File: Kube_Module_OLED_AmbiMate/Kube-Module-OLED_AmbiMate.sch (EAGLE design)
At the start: 9 parts

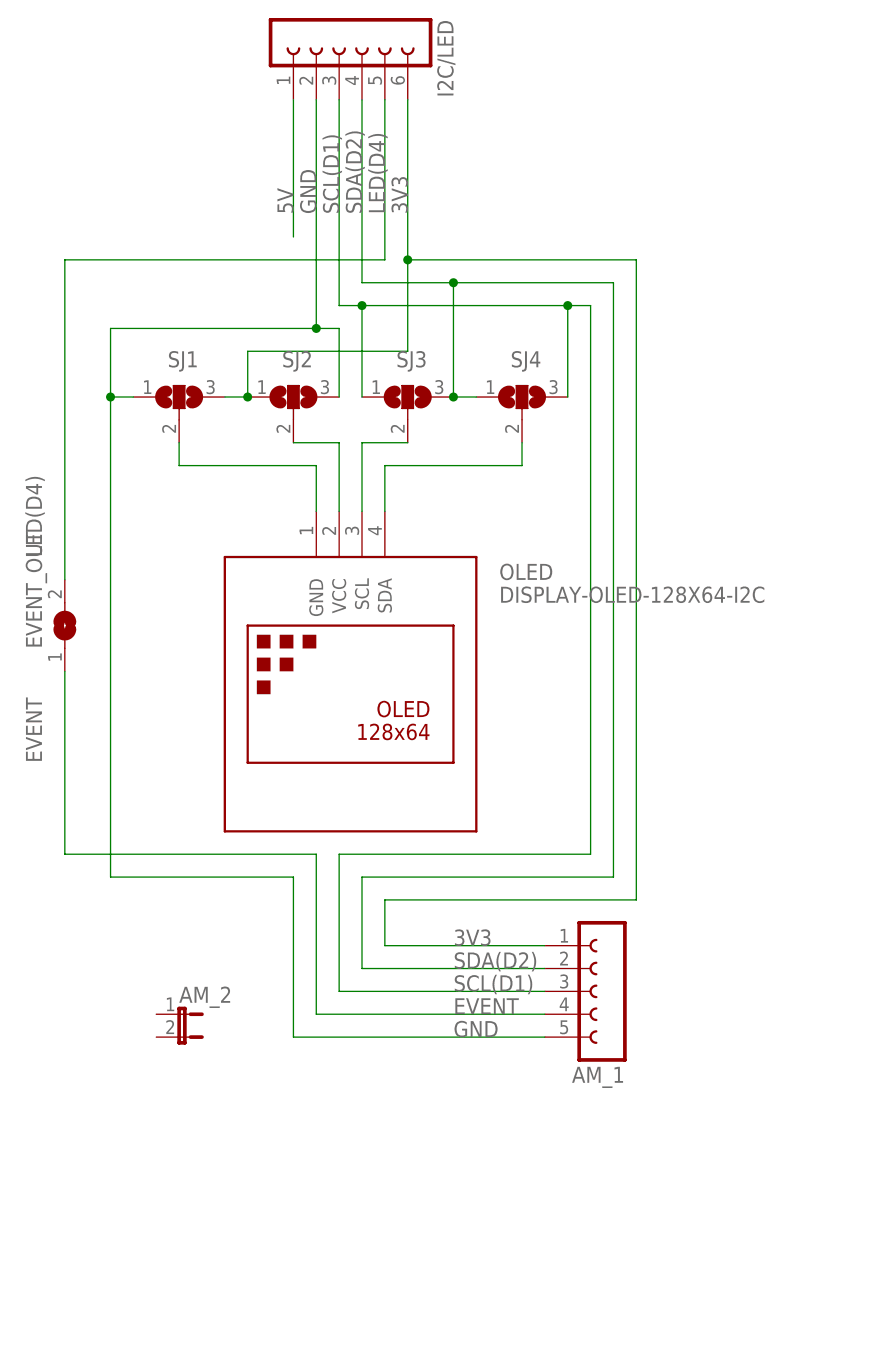
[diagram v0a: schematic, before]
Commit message: Mods to OLED board to get rid of EVENT_OUT (causes boot issues since D4 needs to be held HI)
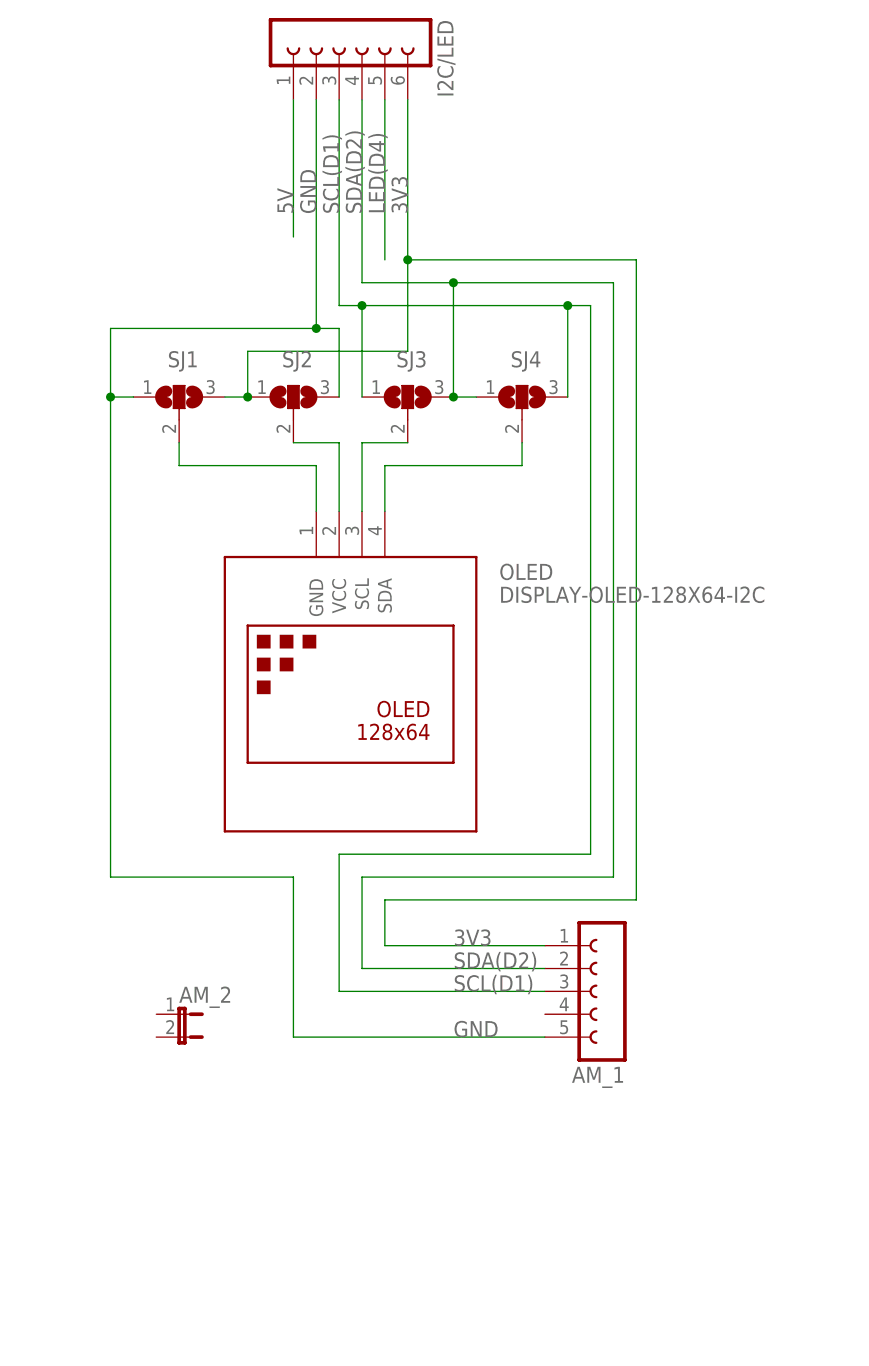
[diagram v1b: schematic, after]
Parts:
- removed EVENT_OUT: (no value), jumper:SJ
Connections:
- removed net EVENT: AM_1.4, EVENT_OUT.1
- net LED(D4): no longer EVENT_OUT.2
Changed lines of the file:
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@@
 <?xml version="1.0" encoding="utf-8"?>
 <!DOCTYPE eagle SYSTEM "eagle.dtd">
-<eagle version="9.3.0">
+<eagle version="9.4.2">
 <drawing>
 <settings>
@@
 <part name="AM_1" library="con-lsta" library_urn="urn:adsk.eagle:library:161" deviceset="FE05-1" device="" package3d_urn="urn:adsk.eagle:package:8190/1"/>
 <part name="AM_2" library="jumper" library_urn="urn:adsk.eagle:library:252" deviceset="JP1E" device="" package3d_urn="urn:adsk.eagle:package:15455/1"/>
-<part name="EVENT_OUT" library="jumper" library_urn="urn:adsk.eagle:library:252" deviceset="SJ" device="" package3d_urn="urn:adsk.eagle:package:15471/1"/>
 </parts>
 <sheets>
@@
 <attribute name="NAME" x="58.42" y="-16.51" size="1.778" layer="95"/>
 <attribute name="VALUE" x="58.42" y="-23.495" size="1.778" layer="96"/>
-</instance>
-<instance part="EVENT_OUT" gate="1" x="45.72" y="25.4" smashed="yes" rot="R90">
-<attribute name="NAME" x="43.18" y="22.86" size="1.778" layer="95" rot="R90"/>
-<attribute name="VALUE" x="49.53" y="22.86" size="1.778" layer="96" rot="R90"/>
 </instance>
 </instances>
@@
 </segment>
 </net>
-<net name="EVENT" class="0">
-<segment>
-<pinref part="AM_1" gate="G$1" pin="4"/>
-<label x="88.9" y="-17.78" size="1.778" layer="95"/>
-<wire x1="99.06" y1="-17.78" x2="73.66" y2="-17.78" width="0.1524" layer="91"/>
-<wire x1="73.66" y1="-17.78" x2="73.66" y2="0" width="0.1524" layer="91"/>
-<wire x1="73.66" y1="0" x2="45.72" y2="0" width="0.1524" layer="91"/>
-<wire x1="45.72" y1="0" x2="45.72" y2="20.32" width="0.1524" layer="91"/>
-<pinref part="EVENT_OUT" gate="1" pin="1"/>
-<label x="43.18" y="10.16" size="1.778" layer="95" rot="R90"/>
-</segment>
-</net>
 <net name="5V" class="0">
 <segment>
@@
 <pinref part="I2C/LED" gate="G$1" pin="5"/>
 <wire x1="81.28" y1="66.04" x2="81.28" y2="83.82" width="0.1524" layer="91"/>
-<wire x1="45.72" y1="66.04" x2="81.28" y2="66.04" width="0.1524" layer="91"/>
-<wire x1="45.72" y1="30.48" x2="45.72" y2="66.04" width="0.1524" layer="91"/>
 <label x="81.28" y="71.12" size="1.778" layer="95" rot="R90"/>
-<pinref part="EVENT_OUT" gate="1" pin="2"/>
-<label x="43.18" y="33.02" size="1.778" layer="95" rot="R90"/>
-</segment>
-</net>
+</segment>
+</net>

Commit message: Added BMx280 sensor to OLED Board
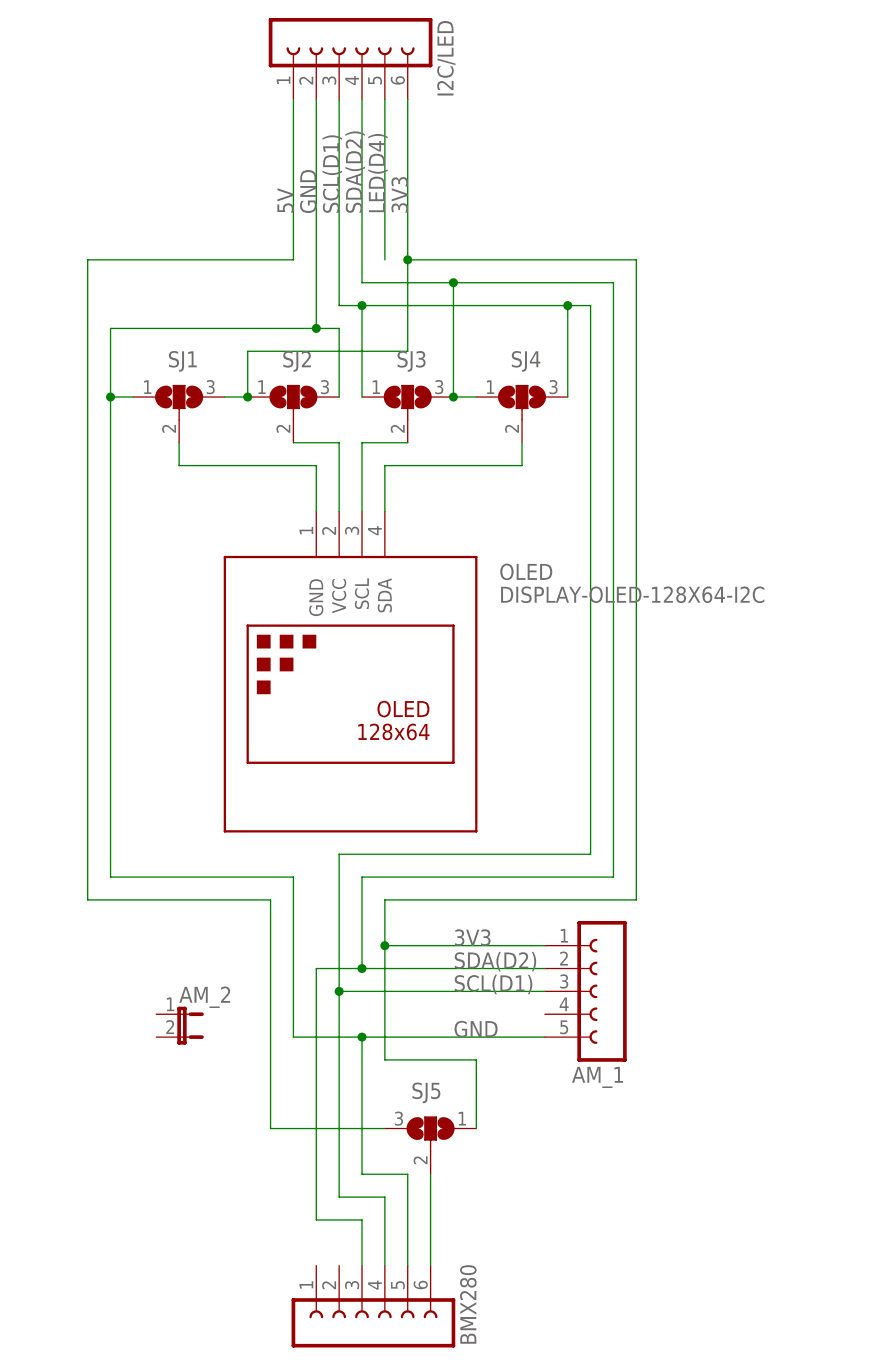
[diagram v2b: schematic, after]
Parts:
- added BMX280: (no value), con-lsta:FE06-1
- added SJ5: (no value), jumper:SJ2W
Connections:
- new net BMX_VCC: BMX280.6, SJ5.2
- net 3V3: now also SJ5.1
- net 5V: now also SJ5.3
- net GND: now also BMX280.5
- net SCL(D1): now also BMX280.4
- net SDA(D2): now also BMX280.3
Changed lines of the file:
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@@
 <?xml version="1.0" encoding="utf-8"?>
 <!DOCTYPE eagle SYSTEM "eagle.dtd">
-<eagle version="9.4.2">
+<eagle version="9.5.2">
 <drawing>
 <settings>
@@
 <part name="AM_1" library="con-lsta" library_urn="urn:adsk.eagle:library:161" deviceset="FE05-1" device="" package3d_urn="urn:adsk.eagle:package:8190/1"/>
 <part name="AM_2" library="jumper" library_urn="urn:adsk.eagle:library:252" deviceset="JP1E" device="" package3d_urn="urn:adsk.eagle:package:15455/1"/>
+<part name="BMX280" library="con-lsta" library_urn="urn:adsk.eagle:library:161" deviceset="FE06-1" device="" package3d_urn="urn:adsk.eagle:package:8191/1"/>
+<part name="SJ5" library="jumper" library_urn="urn:adsk.eagle:library:252" deviceset="SJ2W" device="" package3d_urn="urn:adsk.eagle:package:15474/1"/>
 </parts>
 <sheets>
@@
 <attribute name="NAME" x="58.42" y="-16.51" size="1.778" layer="95"/>
 <attribute name="VALUE" x="58.42" y="-23.495" size="1.778" layer="96"/>
+</instance>
+<instance part="BMX280" gate="G$1" x="78.74" y="-53.34" smashed="yes" rot="MR90">
+<attribute name="VALUE" x="68.58" y="-54.61" size="1.778" layer="96" rot="MR90"/>
+<attribute name="NAME" x="89.662" y="-54.61" size="1.778" layer="95" rot="MR90"/>
+</instance>
+<instance part="SJ5" gate="G$1" x="86.36" y="-30.48" smashed="yes" rot="MR90">
+<attribute name="NAME" x="84.201" y="-25.4" size="1.778" layer="95" rot="MR180"/>
+<attribute name="VALUE" x="84.455" y="-27.94" size="1.778" layer="96" rot="MR90"/>
 </instance>
 </instances>
@@
 <pinref part="AM_1" gate="G$1" pin="5"/>
 <label x="88.9" y="-20.32" size="1.778" layer="95"/>
-<wire x1="99.06" y1="-20.32" x2="71.12" y2="-20.32" width="0.1524" layer="91"/>
+<wire x1="99.06" y1="-20.32" x2="78.74" y2="-20.32" width="0.1524" layer="91"/>
+<wire x1="78.74" y1="-20.32" x2="71.12" y2="-20.32" width="0.1524" layer="91"/>
 <wire x1="71.12" y1="-20.32" x2="71.12" y2="-2.54" width="0.1524" layer="91"/>
 <wire x1="71.12" y1="-2.54" x2="50.8" y2="-2.54" width="0.1524" layer="91"/>
+<wire x1="78.74" y1="-20.32" x2="78.74" y2="-35.56" width="0.1524" layer="91"/>
+<wire x1="78.74" y1="-35.56" x2="83.82" y2="-35.56" width="0.1524" layer="91"/>
+<junction x="78.74" y="-20.32"/>
+<pinref part="BMX280" gate="G$1" pin="5"/>
+<wire x1="83.82" y1="-35.56" x2="83.82" y2="-45.72" width="0.1524" layer="91"/>
 </segment>
 </net>
@@
 <wire x1="99.06" y1="-15.24" x2="76.2" y2="-15.24" width="0.1524" layer="91"/>
 <label x="88.9" y="-15.24" size="1.778" layer="95"/>
+<pinref part="BMX280" gate="G$1" pin="4"/>
+<wire x1="81.28" y1="-45.72" x2="81.28" y2="-38.1" width="0.1524" layer="91"/>
+<wire x1="81.28" y1="-38.1" x2="76.2" y2="-38.1" width="0.1524" layer="91"/>
+<wire x1="76.2" y1="-38.1" x2="76.2" y2="-15.24" width="0.1524" layer="91"/>
+<junction x="76.2" y="-15.24"/>
 </segment>
 </net>
@@
 <label x="88.9" y="-12.7" size="1.778" layer="95"/>
 <wire x1="78.74" y1="-12.7" x2="99.06" y2="-12.7" width="0.1524" layer="91"/>
+<wire x1="78.74" y1="-12.7" x2="73.66" y2="-12.7" width="0.1524" layer="91"/>
+<junction x="78.74" y="-12.7"/>
+<wire x1="73.66" y1="-12.7" x2="73.66" y2="-40.64" width="0.1524" layer="91"/>
+<wire x1="73.66" y1="-40.64" x2="78.74" y2="-40.64" width="0.1524" layer="91"/>
+<pinref part="BMX280" gate="G$1" pin="3"/>
+<wire x1="78.74" y1="-40.64" x2="78.74" y2="-45.72" width="0.1524" layer="91"/>
 </segment>
 </net>
@@
 <wire x1="99.06" y1="-10.16" x2="81.28" y2="-10.16" width="0.1524" layer="91"/>
 <label x="88.9" y="-10.16" size="1.778" layer="95"/>
+<wire x1="81.28" y1="-10.16" x2="81.28" y2="-22.86" width="0.1524" layer="91"/>
+<junction x="81.28" y="-10.16"/>
+<wire x1="81.28" y1="-22.86" x2="91.44" y2="-22.86" width="0.1524" layer="91"/>
+<pinref part="SJ5" gate="G$1" pin="1"/>
+<wire x1="91.44" y1="-22.86" x2="91.44" y2="-30.48" width="0.1524" layer="91"/>
 </segment>
 </net>
@@
 <segment>
 <pinref part="I2C/LED" gate="G$1" pin="1"/>
-<wire x1="71.12" y1="83.82" x2="71.12" y2="68.58" width="0.1524" layer="91"/>
+<wire x1="71.12" y1="83.82" x2="71.12" y2="66.04" width="0.1524" layer="91"/>
 <label x="71.12" y="71.12" size="1.778" layer="95" rot="R90"/>
+<wire x1="71.12" y1="66.04" x2="48.26" y2="66.04" width="0.1524" layer="91"/>
+<wire x1="48.26" y1="66.04" x2="48.26" y2="-5.08" width="0.1524" layer="91"/>
+<wire x1="48.26" y1="-5.08" x2="68.58" y2="-5.08" width="0.1524" layer="91"/>
+<wire x1="68.58" y1="-5.08" x2="68.58" y2="-30.48" width="0.1524" layer="91"/>
+<pinref part="SJ5" gate="G$1" pin="3"/>
+<wire x1="68.58" y1="-30.48" x2="81.28" y2="-30.48" width="0.1524" layer="91"/>
 </segment>
 </net>
@@
 </segment>
 </net>
+<net name="BMX_VCC" class="0">
+<segment>
+<pinref part="BMX280" gate="G$1" pin="6"/>
+<pinref part="SJ5" gate="G$1" pin="2"/>
+<wire x1="86.36" y1="-45.72" x2="86.36" y2="-35.56" width="0.1524" layer="91"/>
+</segment>
+</net>
 </nets>
 </sheet>
 </sheets>
+<errors>
+</errors>
 </schematic>
 </drawing>
